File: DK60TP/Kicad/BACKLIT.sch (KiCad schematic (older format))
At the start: 85 parts, among them U1 PAM2804

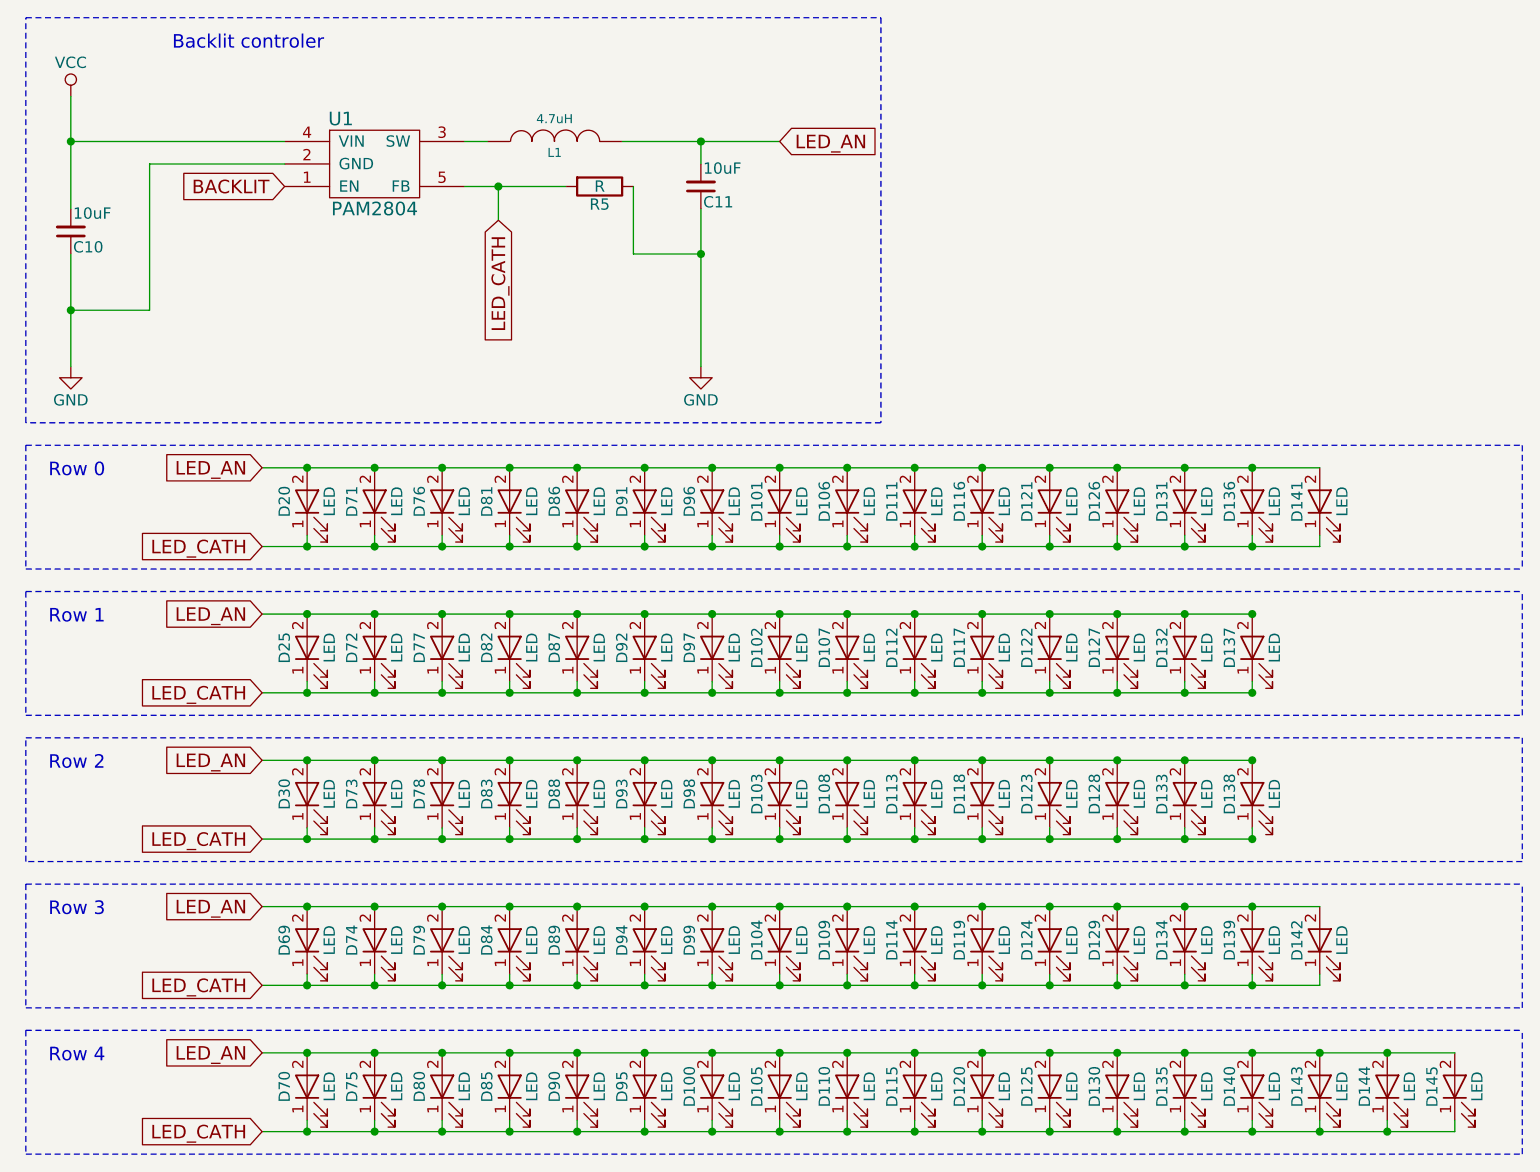
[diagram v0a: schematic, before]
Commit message: - DK60TP: Updated layout possibility - DK60TP: Split schematic in some files
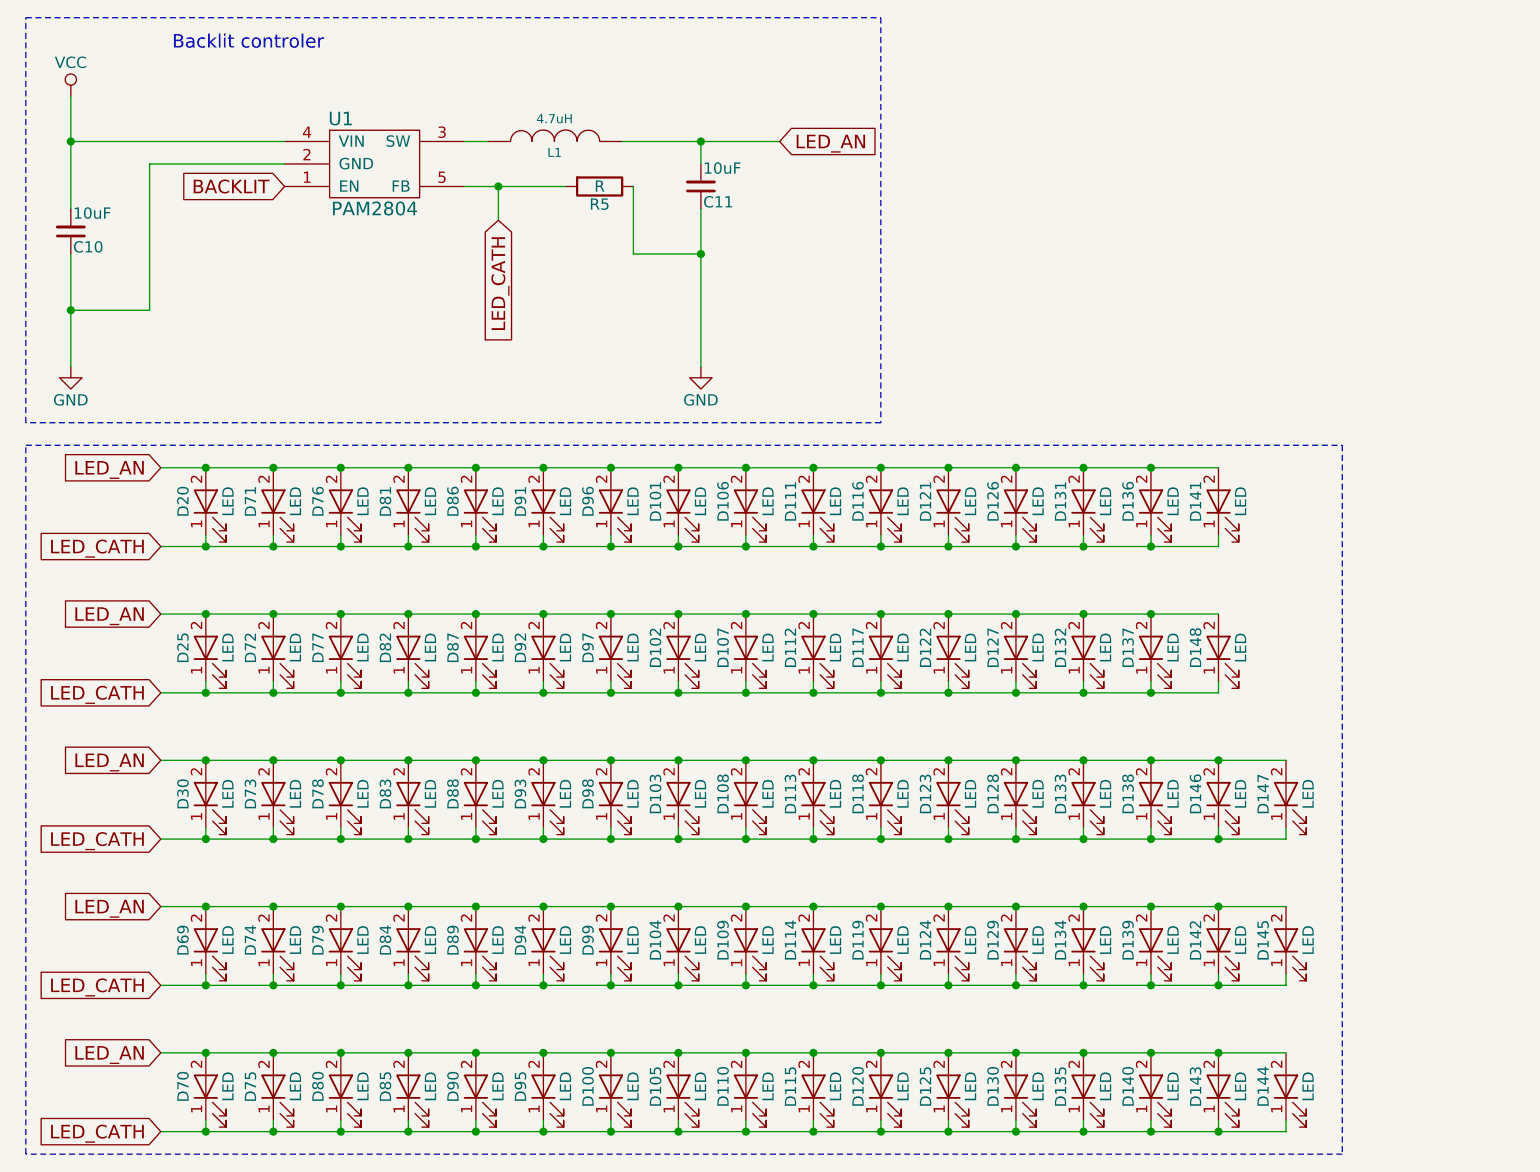
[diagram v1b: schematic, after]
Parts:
- added D146, D147, D148: LED, Footprint:LED_TH_BIVAR, symbol LED
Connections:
- net LED_AN: now also D146.2 (A), D147.2 (A), D148.2 (A)
- net LED_CATH: now also D146.1 (K), D147.1 (K), D148.1 (K)
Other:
- note removed: "Row 0"
- note removed: "Row 1"
- note removed: "Row 2"
- note removed: "Row 3"
- note removed: "Row 4"
- moved on the sheet: D100, D101, D102, D103, D104, D105, D106, D107, D108, D109, D110, D111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

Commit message: - DK60TP: Some changes on PCB (routing)
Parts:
- R5: value R -> 0.5
